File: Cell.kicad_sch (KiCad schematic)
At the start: 19 parts

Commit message: Updated sch, re-create pcb next
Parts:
- R3: renamed from R25; footprint Resistor_THT:R_Axial_DIN0207_L6.3mm_D2.5mm_P7.62mm_Horizontal -> YoshLibrary:R_Axial_DIN0207_L6.3mm_D2.5mm_P7.62mm_Horizontal
- R4: renamed from R26; footprint Resistor_THT:R_Axial_DIN0207_L6.3mm_D2.5mm_P7.62mm_Horizontal -> YoshLibrary:R_Axial_DIN0207_L6.3mm_D2.5mm_P7.62mm_Horizontal
- R5: renamed from R27; footprint Resistor_THT:R_Axial_DIN0207_L6.3mm_D2.5mm_P7.62mm_Horizontal -> YoshLibrary:R_Axial_DIN0207_L6.3mm_D2.5mm_P7.62mm_Horizontal
- R6: renamed from R28; footprint Resistor_THT:R_Axial_DIN0207_L6.3mm_D2.5mm_P7.62mm_Horizontal -> YoshLibrary:R_Axial_DIN0207_L6.3mm_D2.5mm_P7.62mm_Horizontal
- R7: renamed from R29; footprint Resistor_THT:R_Axial_DIN0207_L6.3mm_D2.5mm_P7.62mm_Horizontal -> YoshLibrary:R_Axial_DIN0207_L6.3mm_D2.5mm_P7.62mm_Horizontal
- renumbered D17 to D1, D18 to D2, NQ65 to NQ26, NQ66 to NQ27, NQ67 to NQ28, NQ68 to NQ29, NQ69 to NQ30, NQ70 to NQ31, NQ71 to NQ32, NX1 to NX5, PQ23 to PQ14, PQ24 to PQ15

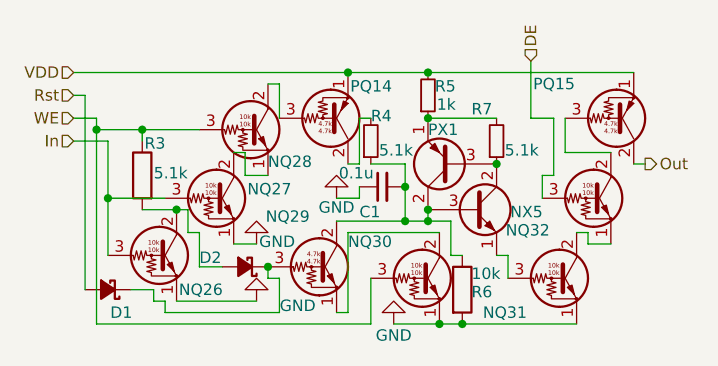
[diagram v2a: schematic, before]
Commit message: Changed size, 1 inst per board. Updating everything
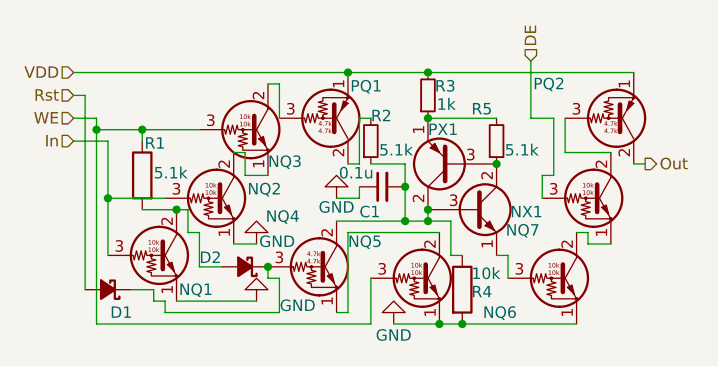
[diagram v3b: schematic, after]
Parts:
- renumbered NQ26 to NQ1, NQ27 to NQ2, NQ28 to NQ3, NQ29 to NQ4, NQ30 to NQ5, NQ31 to NQ6, NQ32 to NQ7, NX5 to NX1, PQ14 to PQ1, PQ15 to PQ2, R3 to R1, R4 to R2, R5 to R3, R6 to R4, R7 to R5

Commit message: Optimized for univ. board
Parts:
- NQ1, NQ2, NQ3, NQ4, NQ5, NQ6, NQ7, NX1, PQ1, PQ2, PX1: footprint Package_TO_SOT_THT:TO-92_Inline -> Package_TO_SOT_THT:TO-92_Inline_Wide
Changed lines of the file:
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@@
 			)
 		)
-		(property "Footprint" "Package_TO_SOT_THT:TO-92_Inline"
+		(property "Footprint" "Package_TO_SOT_THT:TO-92_Inline_Wide"
 			(at 26.67 40.64 0)
 			(effects
@@
 			)
 		)
-		(property "Footprint" "Package_TO_SOT_THT:TO-92_Inline"
+		(property "Footprint" "Package_TO_SOT_THT:TO-92_Inline_Wide"
 			(at 33.02 34.29 0)
 			(effects
@@
 			)
 		)
-		(property "Footprint" "Package_TO_SOT_THT:TO-92_Inline"
+		(property "Footprint" "Package_TO_SOT_THT:TO-92_Inline_Wide"
 			(at 44.45 41.91 0)
 			(effects
@@
 			)
 		)
-		(property "Footprint" "Package_TO_SOT_THT:TO-92_Inline"
+		(property "Footprint" "Package_TO_SOT_THT:TO-92_Inline_Wide"
 			(at 36.83 26.67 0)
 			(effects
@@
 			)
 		)
-		(property "Footprint" "Package_TO_SOT_THT:TO-92_Inline"
+		(property "Footprint" "Package_TO_SOT_THT:TO-92_Inline_Wide"
 			(at 71.12 43.18 0)
 			(effects
@@
 			)
 		)
-		(property "Footprint" "Package_TO_SOT_THT:TO-92_Inline"
+		(property "Footprint" "Package_TO_SOT_THT:TO-92_Inline_Wide"
 			(at 77.47 25.4 0)
 			(effects
@@
 			)
 		)
-		(property "Footprint" "Package_TO_SOT_THT:TO-92_Inline"
+		(property "Footprint" "Package_TO_SOT_THT:TO-92_Inline_Wide"
 			(at 55.88 43.18 0)
 			(effects
@@
 			)
 		)
-		(property "Footprint" "Package_TO_SOT_THT:TO-92_Inline"
+		(property "Footprint" "Package_TO_SOT_THT:TO-92_Inline_Wide"
 			(at 54.61 28.575 0)
 			(effects
@@
 			)
 		)
-		(property "Footprint" "Package_TO_SOT_THT:TO-92_Inline"
+		(property "Footprint" "Package_TO_SOT_THT:TO-92_Inline_Wide"
 			(at 45.72 25.4 0)
 			(effects
@@
 			)
 		)
-		(property "Footprint" "Package_TO_SOT_THT:TO-92_Inline"
+		(property "Footprint" "Package_TO_SOT_THT:TO-92_Inline_Wide"
 			(at 67.31 37.465 0)
 			(effects
@@
 			)
 		)
-		(property "Footprint" "Package_TO_SOT_THT:TO-92_Inline"
+		(property "Footprint" "Package_TO_SOT_THT:TO-92_Inline_Wide"
 			(at 74.93 34.29 0)
 			(effects

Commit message: Did some stuff, started wiring
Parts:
- PQ1, PQ2: value DTA143E-THT -> DTA114E-THT; footprint Package_TO_SOT_THT:TO-92_Inline_Wide -> Package_TO_SOT_THT:TO-92_Inline; symbol YoshLibrary:DTA143E-THT -> YoshLibrary:DTA114E-THT

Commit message: Editing board, size-optimizing
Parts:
- PQ1, PQ2: footprint Package_TO_SOT_THT:TO-92_Inline -> Package_TO_SOT_THT:TO-92_Inline_Wide
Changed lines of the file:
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@@
 			)
 		)
-		(property "Footprint" "Package_TO_SOT_THT:TO-92_Inline"
+		(property "Footprint" "Package_TO_SOT_THT:TO-92_Inline_Wide"
 			(at 77.47 25.4 0)
 			(effects
@@
 			)
 		)
-		(property "Footprint" "Package_TO_SOT_THT:TO-92_Inline"
+		(property "Footprint" "Package_TO_SOT_THT:TO-92_Inline_Wide"
 			(at 45.72 25.4 0)
 			(effects

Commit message: Moved a bit, updated things.csv
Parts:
- D1, D2: value 30V0.2A -> Schottky
- NQ5: value DTC143E-THT -> DTC114E-THT
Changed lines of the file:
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@@
 			)
 		)
-		(property "Value" "DTC143E-THT"
+		(property "Value" "DTC114E-THT"
 			(at 60.96 44.4499 0)
 			(effects
@@
 			)
 		)
-		(property "Value" "30V0.2A"
+		(property "Value" "Schottky"
 			(at 38.3539 39.37 90)
 			(effects
@@
 			)
 		)
-		(property "Value" "30V0.2A"
+		(property "Value" "Schottky"
 			(at 23.1139 41.91 90)
 			(effects
